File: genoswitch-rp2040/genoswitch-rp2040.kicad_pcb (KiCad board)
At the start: 2 copper layers, 43.4 x 57.3 mm, 44 parts, among them J1 USB_B_Micro, J10 RP2040_ADC2, J11 RP2040_ADC3, J2 Conn_01x03_Socket-PicoDebug, J3 HW-SPI0, J4 HW-SPI1, J5 PIO-SPI0, J6 PIO-SPI1, J7 SERIAL, J8 RP2040_ADC0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

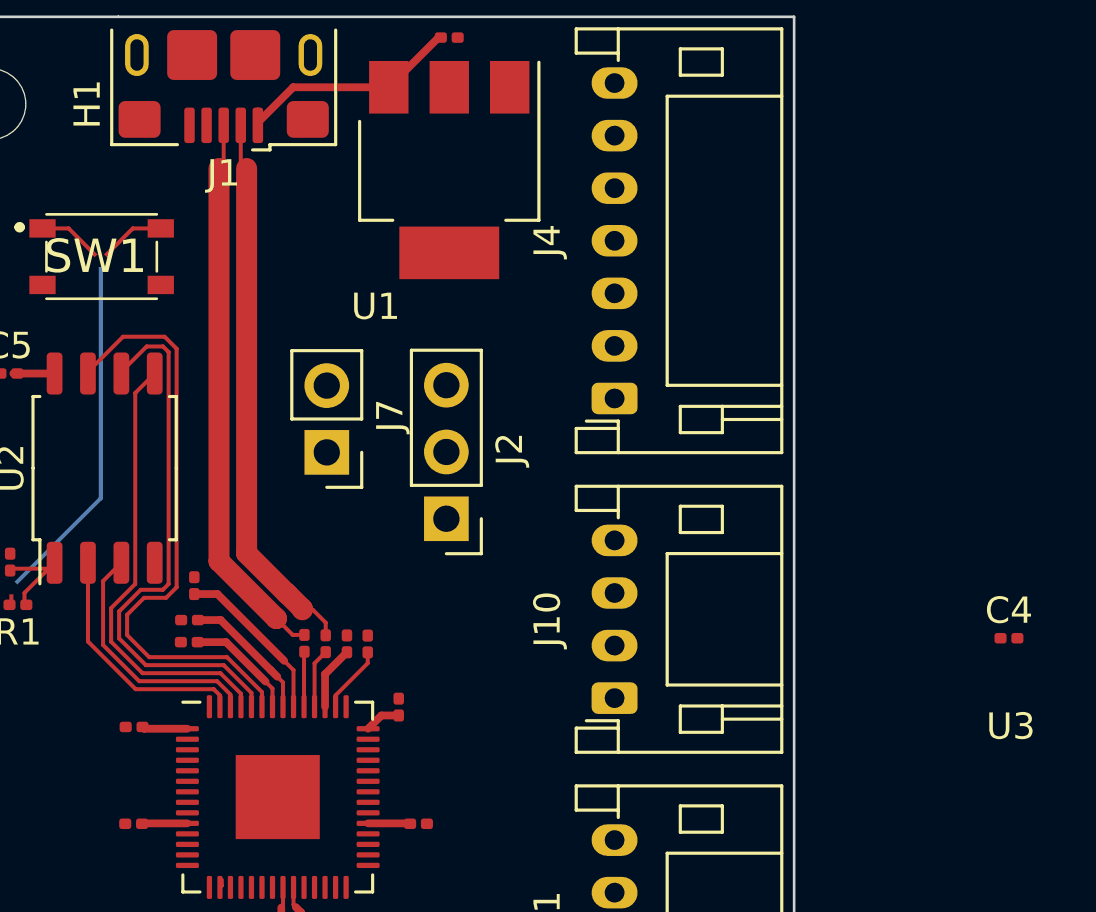
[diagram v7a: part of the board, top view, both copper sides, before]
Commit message: Place capacitor C4, move U1 text
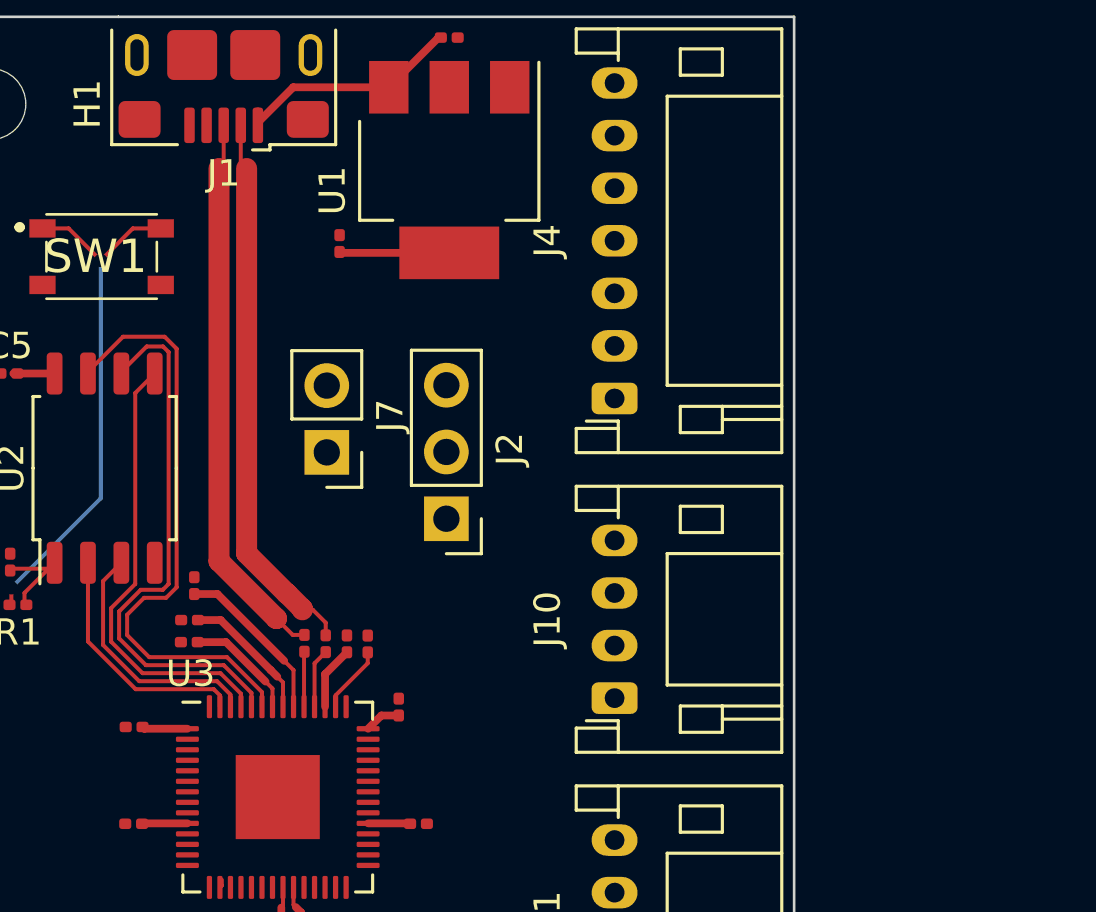
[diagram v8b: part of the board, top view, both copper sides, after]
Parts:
- moved C4 29.6 mm to (111.7, 52.9), turned to 90 degrees
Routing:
- net +3V3: track 1.57 -> 5.76 mm
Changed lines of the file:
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@@
     (property "ki_keywords" "REGULATOR LDO 3.3V")
     (attr smd)
-    (fp_text reference "U1" (at 5.2 2.8 -180) (layer "F.SilkS")
+    (fp_text reference "U1" (at 0.78 4.442 90) (layer "F.SilkS")
         (effects (font (size 1 1) (thickness 0.15)))
     )
@@
   )
   (footprint "Capacitor_SMD:C_0201_0603Metric" (layer "F.Cu")
-    (at 137.165 67.871)
+    (at 111.7 52.855 90)
     (descr "Capacitor SMD 0201 (0603 Metric), square (rectangular) end terminal, IPC_7351 nominal, (Body size source: https://www.vishay.com/docs/20052/crcw0201e3.pdf), generated with kicad-footprint-generator")
     (tags "capacitor")
@@
     (property "ki_keywords" "cap capacitor")
     (attr smd)
-    (fp_text reference "C4" (at 0 -1.05) (layer "F.SilkS")
-        (effects (font (size 1 1) (thickness 0.15)))
-    )
-    (fp_text value "10μF" (at 0 1.05) (layer "F.Fab")
-        (effects (font (size 1 1) (thickness 0.15)))
-    )
-    (fp_text user "${REFERENCE}" (at 0 -0.68) (layer "F.Fab")
+    (fp_text reference "C4" (at 0 -1.05 90) (layer "F.SilkS") hide
+        (effects (font (size 1 1) (thickness 0.15)))
+    )
+    (fp_text value "10μF" (at 0 1.05 90) (layer "F.Fab")
+        (effects (font (size 1 1) (thickness 0.15)))
+    )
+    (fp_text user "${REFERENCE}" (at 0 -0.68 90) (layer "F.Fab")
         (effects (font (size 0.25 0.25) (thickness 0.04)))
     )
@@
     (fp_line (start 0.3 0.15) (end -0.3 0.15)
       (stroke (width 0.1) (type solid)) (layer "F.Fab"))
-    (pad "" smd roundrect (at -0.345 0) (size 0.318 0.36) (layers "F.Paste") (roundrect_rratio 0.25))
-    (pad "" smd roundrect (at 0.345 0) (size 0.318 0.36) (layers "F.Paste") (roundrect_rratio 0.25))
-    (pad "1" smd roundrect (at -0.32 0) (size 0.46 0.4) (layers "F.Cu" "F.Mask") (roundrect_rratio 0.25)
+    (pad "" smd roundrect (at -0.345 0 90) (size 0.318 0.36) (layers "F.Paste") (roundrect_rratio 0.25))
+    (pad "" smd roundrect (at 0.345 0 90) (size 0.318 0.36) (layers "F.Paste") (roundrect_rratio 0.25))
+    (pad "1" smd roundrect (at -0.32 0 90) (size 0.46 0.4) (layers "F.Cu" "F.Mask") (roundrect_rratio 0.25)
       (net 5 "+3V3") (pintype "passive"))
-    (pad "2" smd roundrect (at 0.32 0) (size 0.46 0.4) (layers "F.Cu" "F.Mask") (roundrect_rratio 0.25)
+    (pad "2" smd roundrect (at 0.32 0 90) (size 0.46 0.4) (layers "F.Cu" "F.Mask") (roundrect_rratio 0.25)
       (net 2 "GND") (pintype "passive"))
     (model "${KICAD6_3DMODEL_DIR}/Capacitor_SMD.3dshapes/C_0201_0603Metric.wrl"
@@
     (property "ki_keywords" "RP2040 ARM Cortex-M0+ USB")
     (attr smd)
-    (fp_text reference "U3" (at 27.888 -2.684) (layer "F.SilkS")
+    (fp_text reference "U3" (at -3.317 -4.694) (layer "F.SilkS")
         (effects (font (size 1 1) (thickness 0.15)))
     )
@@
   (segment (start 114.366 74.914) (end 114.382 74.93) (width 0.295656) (layer "F.Cu") (net 2))
   (segment (start 109.947 70.4765) (end 109.947 69.085) (width 0.1524) (layer "F.Cu") (net 2))
+  (segment (start 111.735 53.21) (end 111.7 53.175) (width 0.295656) (layer "F.Cu") (net 5))
+  (segment (start 115.872 53.21) (end 111.735 53.21) (width 0.295656) (layer "F.Cu") (net 5))
   (segment (start 100.857 57.8) (end 99.287 57.8) (width 0.295656) (layer "F.Cu") (net 5))
   (segment (start 107.382 68.02) (end 108.882 69.52) (width 0.295656) (layer "F.Cu") (net 6))
